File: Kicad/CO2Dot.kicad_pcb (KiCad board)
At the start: 4 copper layers, 25 x 25 mm, 20 parts, among them J1 Conn_01x08, J3 Conn_01x02_Socket, U1 AS7341/3, U4 BME680, U5 AP7312-1833W6-7, U8 ESP8685, Y2 40MHz

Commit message: PCB CO2Dot with BME, V002 (squashed)
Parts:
- removed J1: Conn_01x08, Connector_FFC-FPC:Molex_5034800800_1x08-1MP_P0.50mm_Horizontal
- removed J3: Conn_01x02_Socket, Connector_PinHeader_2.54mm:PinHeader_1x02_P2.54mm_Vertical
- removed R1: 500, Resistor_SMD:R_0603_1608Metric_Pad0.98x0.95mm_HandSolder
- removed R4, R5: 10K, Resistor_SMD:R_0603_1608Metric_Pad0.98x0.95mm_HandSolder
- removed U4: BME680, Package_LGA:Bosch_LGA-8_3x3mm_P0.8mm_ClockwisePinNumbering
- added C1: 2.2u, Capacitor_SMD:C_0603_1608Metric_Pad1.08x0.95mm_HandSolder, F.Cu at (106.9, 80.0)
- added C4: 2.2u, Capacitor_SMD:C_0603_1608Metric_Pad1.08x0.95mm_HandSolder, F.Cu at (92.6, 93.3)
- added C6: 10u, Capacitor_SMD:C_0603_1608Metric, F.Cu at (96.5, 81.3)
- added D1: 1N4148WT, Diode_SMD:D_SOD-123, F.Cu at (95.5, 83.3)
- added D3: LED, Diode_SMD:D_0805_2012Metric, F.Cu at (96.2, 85.7)
- added J2: USB_C_Receptacle, Connector_USB:USB_C_Receptacle_HRO_TYPE-C-31-M-12, F.Cu at (100.0, 75.0)
- added J4: Conn_01x02_Pin, Connector_PinHeader_2.54mm:PinHeader_1x02_P2.54mm_Vertical, F.Cu at (106.6, 83.6)
- added J5: secondBoard, Connector_PinSocket_1.27mm:PinSocket_1x04_P1.27mm_Vertical, F.Cu at (100.1, 109.6)
- added R12: 5.1K, Resistor_SMD:R_0603_1608Metric, F.Cu at (106.2, 86.6)
- added R13: 5.1K, Resistor_SMD:R_0603_1608Metric, F.Cu at (95.0, 89.0)
- added R29: 5.1K, Resistor_SMD:R_0603_1608Metric, F.Cu at (90.8, 82.8)
- added R30: 5.1K, Resistor_SMD:R_0603_1608Metric, F.Cu at (92.3, 82.8)
- added R7: 10K, Resistor_SMD:R_0603_1608Metric_Pad0.98x0.95mm_HandSolder, F.Cu at (96.7, 93.3)
- added R8: 10K, Resistor_SMD:R_0603_1608Metric_Pad0.98x0.95mm_HandSolder, F.Cu at (100.7, 93.3)
- added SW2: SW_Push, Button_Switch_SMD:SW_SPST_EVQP2_ShortPushTravel_H2.1mm, F.Cu at (109.9, 89.4)
- added U2: IP4234CZ6, Package_TO_SOT_SMD:SC-74-6_1.55x2.9mm_P0.95mm, F.Cu at (100.3, 83.6)
- added U3: BME688, Personal_Library:BME688, F.Cu at (94.9, 100.4)
- C2, C9: value 100n -> 2.2u
- D2: footprint Personal_Library:NF2W757GT-F1 -> Diode_SMD:D_0805_2012Metric
- R2: value 10K -> 5.1K; footprint Resistor_SMD:R_0603_1608Metric_Pad0.98x0.95mm_HandSolder -> Resistor_SMD:R_0603_1608Metric
- R3: value 10K -> 0R
- R6: value 12K -> 0R
- U1: value AS7341/3 -> AS7341-DLGT; footprint Personal_Library:XDCR_AS7341-DLGM -> ambit_library:PSON80P310X200X110-8N
- U5: footprint Package_TO_SOT_SMD:TSOT-23-6_HandSoldering -> Package_TO_SOT_SMD:TSOT-23-6
- moved C2 152.1 mm to (93.5, 86.5), turned to 90 degrees
- moved R6 147.6 mm to (104.4, 93.3), turned to 0 degrees
- moved C12 142.6 mm to (91.6, 86.5), turned to 90 degrees
- moved C10 142.6 mm to (103.9, 83.7), turned to 90 degrees
- moved R2 141.9 mm to (106.1, 88.1)
- moved U5 141.9 mm to (92.3, 90.4), turned to -90 degrees
- moved C3 141.8 mm to (96.6, 91.8)
- moved U8 141.2 mm to (101.7, 88.9)
- moved C11 141.1 mm to (106.9, 90.7), turned to -90 degrees
- moved Y2 140.0 mm to (97.5, 89.0), turned to 90 degrees
- moved R3 138.8 mm to (109.2, 93.9), turned to 180 degrees
- moved U1 136.9 mm to (104.8, 100.6)
- moved C9 136.8 mm to (104.9, 103.5)
- moved D2 136.5 mm to (104.8, 97.8), turned to 180 degrees
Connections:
- R3 pad 1: Net-(U8-MTDO/GPIO7) -> SDA_2
- R3 pad 2: SYNC -> SCL
- R6 pad 1: GND -> SCL_2
- R6 pad 2: SYNC -> SDA
- U1 pad 6: SYNC -> unconnected-(U1-GPIO-Pad6)
- U8 pad 13: Net-(U8-MTDO/GPIO7) -> unconnected-(U8-MTDO/GPIO7-Pad13)
- U8 pad 16: GPIO-ADPD -> Net-(D3-A)
- U8 pad 21: unconnected-(U8-GPIO18/USB_D--Pad21) -> D-
- U8 pad 22: unconnected-(U8-GPIO19/USB_D+-Pad22) -> D+
- U8 pad 23: Rxd -> Net-(U8-U0RXD/GPIO20)
- U8 pad 4: unconnected-(U8-GPIO0/XTAL_32K_P/ADC1_CH0-Pad4) -> SDA_2
- U8 pad 5: unconnected-(U8-GPIO1/XTAL_32K_N/ADC1_CH1-Pad5) -> SCL_2
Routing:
- net V+: track 2.75 -> 32.4 mm, vias 0 -> 5
- net SDA_2: track 0.00 -> 29.4 mm, vias 0 -> 1
- net SYNC: track 26.5 -> 0.00 mm, vias 6 -> 0
- net SCL_2: track 0.00 -> 23.3 mm, vias 0 -> 1
- net SCL: track 16.2 -> 36.2 mm, vias 3 -> 4
- net V+3V: track 18.0 -> 36.1 mm, vias 4 -> 6
- net SDA: track 16.5 -> 34.6 mm, vias 2 -> 4
- net Vusb: track 0.00 -> 16.9 mm, vias 0 -> 2
- net V+1.8V: track 21.3 -> 38.2 mm, vias 3 -> 0
- net CC1: track 0.00 -> 16.9 mm, vias 0 -> 2
- net GND: track 19.6 -> 34.9 mm, vias 18 -> 34
- net reset_EN: track 22.1 -> 7.31 mm, vias 4 -> 2
- net CC2: track 0.00 -> 11.6 mm, vias 0 -> 2
- net Rxd: track 9.40 -> 0.00 mm
- net Net-(J2-D+-PadA6): track 0.00 -> 8.56 mm, vias 0 -> 2
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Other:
- board size 25 x 25 mm -> 25 x 40 mm
- board text added: "."
- board text added: "CO2Dot V0.02 LG/LC"
- board text removed: "CO2Dot RZ, LC, LG"
- board text removed: "V+, V+, GND, GND, RST_en, TX, RX, BOOT"

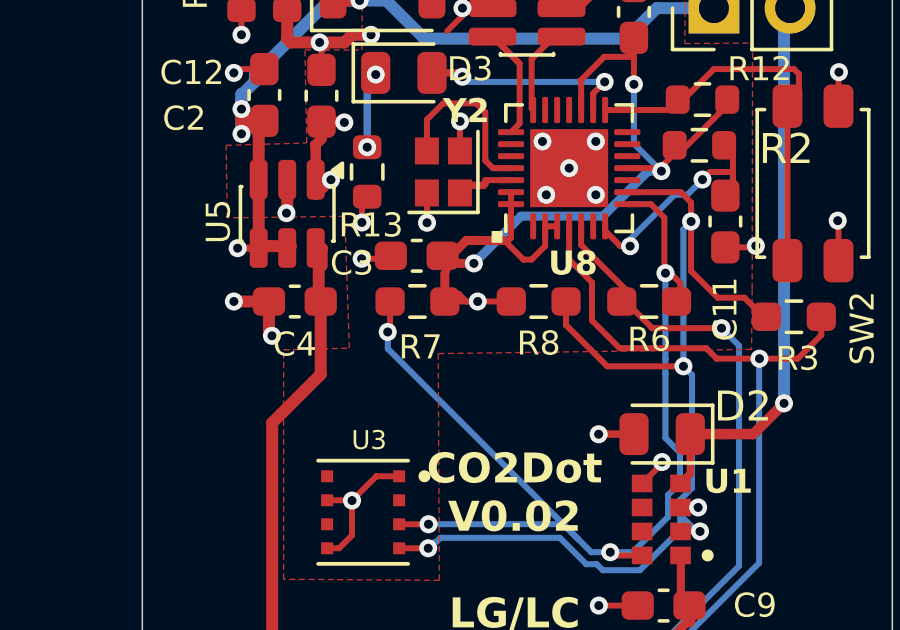
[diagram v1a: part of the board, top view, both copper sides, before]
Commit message: Apply updated .gitignore (untrack now-ignored files)
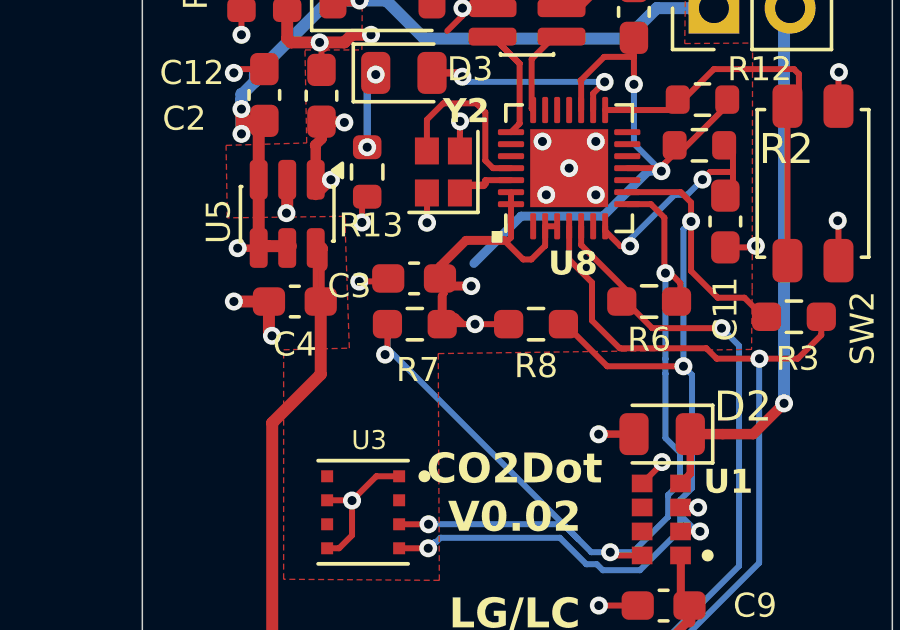
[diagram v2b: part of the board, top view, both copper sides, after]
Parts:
- moved C3 0.76 mm to (96.6, 92.6)
- moved R7 0.76 mm to (96.6, 94.1)
- moved R8 0.76 mm to (100.6, 94.1)
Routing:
- net SCL: track 36.2 -> 35.2 mm
- net V+3V: track 36.1 -> 37.0 mm
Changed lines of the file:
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@@
 	(footprint "Capacitor_SMD:C_0603_1608Metric_Pad1.08x0.95mm_HandSolder"
 		(layer "F.Cu")
-		(at 96.647 91.821 180)
+		(at 96.55925 92.576 180)
 		(descr "Capacitor SMD 0603 (1608 Metric), square (rectangular) end terminal, IPC-7351 nominal with elongated pad for handsoldering. (Body size source: IPC-SM-782 page 76, https://www.pcb-3d.com/wordpress/wp-content/uploads/ipc-sm-782a_amendment_1_and_2.pdf), generated with kicad-footprint-generator")
 		(tags "capacitor handsolder")
@@
 	(footprint "Resistor_SMD:R_0603_1608Metric_Pad0.98x0.95mm_HandSolder"
 		(layer "F.Cu")
-		(at 100.711 93.345 180)
+		(at 100.62325 94.1 180)
 		(descr "Resistor SMD 0603 (1608 Metric), square (rectangular) end terminal, IPC-7351 nominal with elongated pad for handsoldering. (Body size source: IPC-SM-782 page 72, https://www.pcb-3d.com/wordpress/wp-content/uploads/ipc-sm-782a_amendment_1_and_2.pdf), generated with kicad-footprint-generator")
 		(tags "resistor handsolder")
@@
 	(footprint "Resistor_SMD:R_0603_1608Metric_Pad0.98x0.95mm_HandSolder"
 		(layer "F.Cu")
-		(at 96.6705 93.345)
+		(at 96.58275 94.1)
 		(descr "Resistor SMD 0603 (1608 Metric), square (rectangular) end terminal, IPC-7351 nominal with elongated pad for handsoldering. (Body size source: IPC-SM-782 page 72, https://www.pcb-3d.com/wordpress/wp-content/uploads/ipc-sm-782a_amendment_1_and_2.pdf), generated with kicad-footprint-generator")
 		(tags "resistor handsolder")
@@
 	)
 	(segment
-		(start 97.7635 92.075)
-		(end 97.6365 91.948)
+		(start 97.67575 92.83)
+		(end 97.54875 92.703)
 		(width 0.2)
 		(layer "F.Cu")
@@
 	)
 	(segment
-		(start 98.044 93.091)
-		(end 98.298 93.345)
+		(start 97.95625 93.846)
+		(end 98.21025 94.1)
 		(width 0.2)
 		(layer "F.Cu")
@@
 	)
 	(segment
-		(start 99.7985 93.345)
-		(end 98.679 93.345)
+		(start 99.71075 94.1)
+		(end 98.59125 94.1)
 		(width 0.2)
 		(layer "F.Cu")
@@
 	)
 	(segment
-		(start 99.695 91.313)
-		(end 99.7895 91.2185)
+		(start 99.6865 91.308)
+		(end 99.781 91.2135)
 		(width 0.2)
 		(layer "F.Cu")
@@
 	)
 	(segment
-		(start 97.6365 92.3025)
-		(end 97.663 92.329)
+		(start 97.54875 93.0575)
+		(end 97.57525 93.084)
 		(width 0.2)
 		(layer "F.Cu")
@@
 	)
 	(segment
-		(start 97.79 91.821)
-		(end 98.298 91.313)
-		(width 0.3)
-		(layer "F.Cu")
-		(net 1)
-	)
-	(segment
 		(start 94.2075 87.3495)
 		(end 94.234 87.376)
@@
 	)
 	(segment
-		(start 97.5595 93.091)
-		(end 98.044 93.091)
+		(start 97.47175 93.846)
+		(end 97.95625 93.846)
 		(width 0.2)
 		(layer "F.Cu")
@@
 	)
 	(segment
-		(start 98.552 92.075)
-		(end 97.7635 92.075)
+		(start 98.46425 92.83)
+		(end 97.67575 92.83)
+		(width 0.3)
+		(layer "F.Cu")
+		(net 1)
+	)
+	(segment
+		(start 97.42175 92.17575)
+		(end 97.42175 92.576)
 		(width 0.3)
 		(layer "F.Cu")
@@
 	)
 	(segment
-		(start 99.568 91.313)
-		(end 98.298 91.313)
-		(width 0.3)
-		(layer "F.Cu")
-		(net 1)
-	)
-	(segment
-		(start 97.536 93.392)
-		(end 97.583 93.345)
+		(start 97.44825 94.147)
+		(end 97.49525 94.1)
 		(width 0.2)
 		(layer "F.Cu")
@@
 	)
 	(segment
-		(start 97.583 92.409)
-		(end 97.663 92.329)
+		(start 97.49525 93.164)
+		(end 97.57525 93.084)
 		(width 0.2)
 		(layer "F.Cu")
@@
 	)
 	(segment
-		(start 98.679 93.345)
-		(end 97.583 93.345)
+		(start 98.59125 94.1)
+		(end 97.49525 94.1)
 		(width 0.2)
 		(layer "F.Cu")
@@
 	)
 	(segment
-		(start 100.927 91.497)
-		(end 100.476 91.948)
+		(start 100.9185 91.492)
+		(end 100.4675 91.943)
 		(width 0.2)
 		(layer "F.Cu")
@@
 	)
 	(segment
-		(start 97.5095 91.821)
-		(end 97.79 91.821)
+		(start 97.42175 92.576)
+		(end 97.70225 92.576)
 		(width 0.25)
 		(layer "F.Cu")
@@
 	)
 	(segment
-		(start 97.583 93.345)
-		(end 97.583 92.409)
+		(start 97.49525 94.1)
+		(end 97.49525 93.164)
 		(width 0.3)
 		(layer "F.Cu")
@@
 	)
 	(segment
+		(start 98.2895 91.308)
+		(end 97.42175 92.17575)
+		(width 0.3)
+		(layer "F.Cu")
+		(net 1)
+	)
+	(segment
 		(start 99.7895 89.7)
 		(end 99.7895 90.100001)
@@
 	)
 	(segment
-		(start 100.203 91.948)
-		(end 99.568 91.313)
+		(start 100.1945 91.943)
+		(end 99.5595 91.308)
 		(width 0.2)
 		(layer "F.Cu")
@@
 	)
 	(segment
-		(start 100.476 91.948)
-		(end 100.203 91.948)
+		(start 100.4675 91.943)
+		(end 100.1945 91.943)
 		(width 0.2)
 		(layer "F.Cu")
 		(net 1)
 	)
+	(segment
+		(start 99.5595 91.308)
+		(end 98.2895 91.308)
+		(width 0.3)
+		(layer "F.Cu")
+		(net 1)
+	)
 	(via
 		(at 94.234 87.376)
@@
 	)
 	(via
-		(at 98.679 93.345)
+		(at 98.59125 94.1)
 		(size 0.6)
 		(drill 0.3)
@@
 	)
 	(via
-		(at 98.552 92.075)
+		(at 98.46425 92.83)
 		(size 0.6)
 		(drill 0.3)
@@
 	)
 	(segment
-		(start 95.758 94.282)
-		(end 95.758 93.345)
+		(start 95.67025 95.037)
+		(end 95.67025 94.1)
 		(width 0.2)
 		(layer "F.Cu")
@@
 	)
 	(segment
-		(start 95.68 94.36)
-		(end 95.758 94.282)
+		(start 95.59225 95.115)
+		(end 95.67025 95.037)
 		(width 0.2)
 		(layer "F.Cu")
@@
 	)
 	(via
-		(at 95.68 94.36)
+		(at 95.59225 95.115)
 		(size 0.6)
 		(drill 0.3)
@@
 	)
 	(segment
-		(start 101.6235 93.091)
-		(end 101.6235 94.1305)
-		(width 0.2)
-		(layer "F.Cu")
-		(net 3)
-	)
-	(segment
 		(start 101.6235 94.1305)
 		(end 102.997 95.504)
@@
 	)
 	(segment
-		(start 95.6855 91.92)
-		(end 95.7845 91.821)
+		(start 95.59775 92.675)
+		(end 95.69675 92.576)
 		(width 0.2)
 		(layer "F.Cu")
@@
 	)
 	(segment
-		(start 94.81 91.92)
-		(end 95.6855 91.92)
+		(start 94.72225 92.675)
+		(end 95.59775 92.675)
 		(width 0.2)
 		(layer "F.Cu")
@@
 	)
 	(via
-		(at 94.81 91.92)
+		(at 94.73075 92.68)
 		(size 0.6)
 		(drill 0.3)
